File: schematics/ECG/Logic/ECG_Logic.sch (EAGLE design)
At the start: 72 parts, among them IC1 ADS1293, IC2 LIS3DH, IC3 MCP1703, IC4 CC2541, IC5 FSA4157, IC6 FSA4157, IC7 FSA4157, IC8 BALUN_2450BM_SERIES_SMD, X1 XTAL-2SMD, X2 XTAL_403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

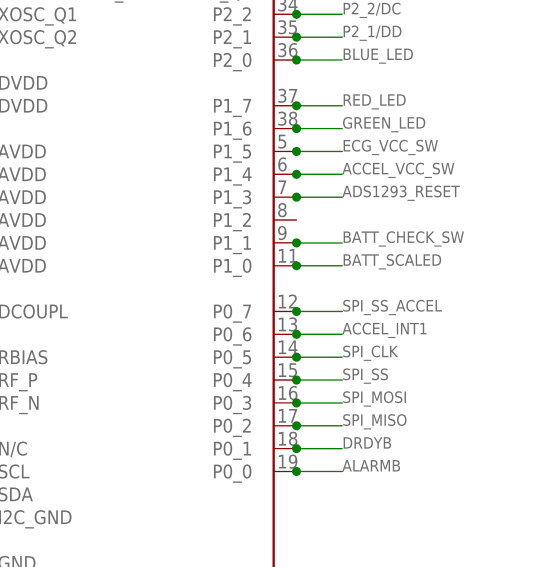
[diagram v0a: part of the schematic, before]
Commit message: moved batt scaled wire to ADC port 0 pin, updated routing. new gerbers generated for ordering v1.0 board
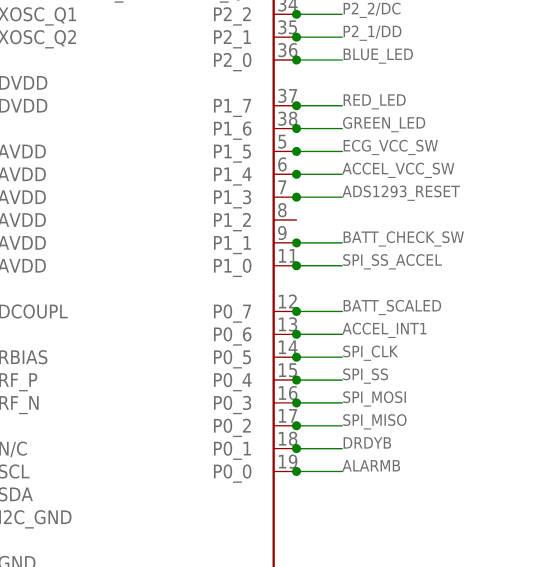
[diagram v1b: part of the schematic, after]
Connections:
- net BATT_SCALED: now also IC4.P0_7; no longer IC4.P1_0
- net SPI_SS_ACCEL: now also IC4.P1_0; no longer IC4.P0_7
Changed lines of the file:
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@@
 <grid distance="0.1" unitdist="inch" unit="inch" style="lines" multiple="1" display="no" altdistance="0.01" altunitdist="inch" altunit="inch"/>
 <layers>
-<layer number="1" name="Top" color="4" fill="1" visible="yes" active="no"/>
-<layer number="2" name="Route2" color="1" fill="3" visible="yes" active="no"/>
-<layer number="3" name="Route3" color="4" fill="3" visible="yes" active="no"/>
-<layer number="4" name="Route4" color="1" fill="4" visible="yes" active="no"/>
-<layer number="5" name="Route5" color="4" fill="4" visible="yes" active="no"/>
-<layer number="6" name="Route6" color="1" fill="8" visible="yes" active="no"/>
-<layer number="7" name="Route7" color="4" fill="8" visible="yes" active="no"/>
-<layer number="8" name="Route8" color="1" fill="2" visible="yes" active="no"/>
-<layer number="9" name="Route9" color="4" fill="2" visible="yes" active="no"/>
-<layer number="10" name="Route10" color="1" fill="7" visible="yes" active="no"/>
-<layer number="11" name="Route11" color="4" fill="7" visible="yes" active="no"/>
-<layer number="12" name="Route12" color="1" fill="5" visible="yes" active="no"/>
-<layer number="13" name="Route13" color="4" fill="5" visible="yes" active="no"/>
-<layer number="14" name="Route14" color="1" fill="6" visible="yes" active="no"/>
-<layer number="15" name="Route15" color="4" fill="6" visible="yes" active="no"/>
-<layer number="16" name="Bottom" color="1" fill="1" visible="yes" active="no"/>
-<layer number="17" name="Pads" color="2" fill="1" visible="yes" active="no"/>
-<layer number="18" name="Vias" color="2" fill="1" visible="yes" active="no"/>
-<layer number="19" name="Unrouted" color="6" fill="1" visible="yes" active="no"/>
-<layer number="20" name="Dimension" color="15" fill="1" visible="yes" active="no"/>
-<layer number="21" name="tPlace" color="7" fill="1" visible="yes" active="no"/>
-<layer number="22" name="bPlace" color="7" fill="1" visible="yes" active="no"/>
-<layer number="23" name="tOrigins" color="15" fill="1" visible="yes" active="no"/>
-<layer number="24" name="bOrigins" color="15" fill="1" visible="yes" active="no"/>
-<layer number="25" name="tNames" color="7" fill="1" visible="yes" active="no"/>
-<layer number="26" name="bNames" color="7" fill="1" visible="yes" active="no"/>
-<layer number="27" name="tValues" color="7" fill="1" visible="yes" active="no"/>
-<layer number="28" name="bValues" color="7" fill="1" visible="yes" active="no"/>
+<layer number="1" name="Top" color="4" fill="1" visible="no" active="no"/>
+<layer number="2" name="Route2" color="1" fill="3" visible="no" active="no"/>
+<layer number="3" name="Route3" color="4" fill="3" visible="no" active="no"/>
+<layer number="4" name="Route4" color="1" fill="4" visible="no" active="no"/>
+<layer number="5" name="Route5" color="4" fill="4" visible="no" active="no"/>
+<layer number="6" name="Route6" color="1" fill="8" visible="no" active="no"/>
+<layer number="7" name="Route7" color="4" fill="8" visible="no" active="no"/>
+<layer number="8" name="Route8" color="1" fill="2" visible="no" active="no"/>
+<layer number="9" name="Route9" color="4" fill="2" visible="no" active="no"/>
+<layer number="10" name="Route10" color="1" fill="7" visible="no" active="no"/>
+<layer number="11" name="Route11" color="4" fill="7" visible="no" active="no"/>
+<layer number="12" name="Route12" color="1" fill="5" visible="no" active="no"/>
+<layer number="13" name="Route13" color="4" fill="5" visible="no" active="no"/>
+<layer number="14" name="Route14" color="1" fill="6" visible="no" active="no"/>
+<layer number="15" name="Route15" color="4" fill="6" visible="no" active="no"/>
+<layer number="16" name="Bottom" color="1" fill="1" visible="no" active="no"/>
+<layer number="17" name="Pads" color="2" fill="1" visible="no" active="no"/>
+<layer number="18" name="Vias" color="2" fill="1" visible="no" active="no"/>
+<layer number="19" name="Unrouted" color="6" fill="1" visible="no" active="no"/>
+<layer number="20" name="Dimension" color="15" fill="1" visible="no" active="no"/>
+<layer number="21" name="tPlace" color="7" fill="1" visible="no" active="no"/>
+<layer number="22" name="bPlace" color="7" fill="1" visible="no" active="no"/>
+<layer number="23" name="tOrigins" color="15" fill="1" visible="no" active="no"/>
+<layer number="24" name="bOrigins" color="15" fill="1" visible="no" active="no"/>
+<layer number="25" name="tNames" color="7" fill="1" visible="no" active="no"/>
+<layer number="26" name="bNames" color="7" fill="1" visible="no" active="no"/>
+<layer number="27" name="tValues" color="7" fill="1" visible="no" active="no"/>
+<layer number="28" name="bValues" color="7" fill="1" visible="no" active="no"/>
 <layer number="29" name="tStop" color="7" fill="3" visible="no" active="no"/>
 <layer number="30" name="bStop" color="7" fill="6" visible="no" active="no"/>
@@
 <layer number="35" name="tGlue" color="7" fill="4" visible="no" active="no"/>
 <layer number="36" name="bGlue" color="7" fill="5" visible="no" active="no"/>
-<layer number="37" name="tTest" color="7" fill="1" visible="yes" active="no"/>
-<layer number="38" name="bTest" color="7" fill="1" visible="yes" active="no"/>
+<layer number="37" name="tTest" color="7" fill="1" visible="no" active="no"/>
+<layer number="38" name="bTest" color="7" fill="1" visible="no" active="no"/>
 <layer number="39" name="tKeepout" color="4" fill="11" visible="no" active="no"/>
 <layer number="40" name="bKeepout" color="1" fill="11" visible="no" active="no"/>
@@
 <layer number="44" name="Drills" color="7" fill="1" visible="no" active="no"/>
 <layer number="45" name="Holes" color="7" fill="1" visible="no" active="no"/>
-<layer number="46" name="Milling" color="3" fill="1" visible="yes" active="no"/>
-<layer number="47" name="Measures" color="7" fill="1" visible="yes" active="no"/>
-<layer number="48" name="Document" color="7" fill="1" visible="yes" active="no"/>
-<layer number="49" name="Reference" color="7" fill="1" visible="yes" active="no"/>
-<layer number="50" name="dxf" color="7" fill="1" visible="yes" active="no"/>
-<layer number="51" name="tDocu" color="7" fill="1" visible="yes" active="no"/>
-<layer number="52" name="bDocu" color="7" fill="1" visible="yes" active="no"/>
-<layer number="53" name="tGND_GNDA" color="7" fill="9" visible="yes" active="no"/>
-<layer number="54" name="bGND_GNDA" color="1" fill="9" visible="yes" active="no"/>
-<layer number="56" name="wert" color="7" fill="1" visible="yes" active="no"/>
+<layer number="46" name="Milling" color="3" fill="1" visible="no" active="no"/>
+<layer number="47" name="Measures" color="7" fill="1" visible="no" active="no"/>
+<layer number="48" name="Document" color="7" fill="1" visible="no" active="no"/>
+<layer number="49" name="Reference" color="7" fill="1" visible="no" active="no"/>
+<layer number="50" name="dxf" color="7" fill="1" visible="no" active="no"/>
+<layer number="51" name="tDocu" color="7" fill="1" visible="no" active="no"/>
+<layer number="52" name="bDocu" color="7" fill="1" visible="no" active="no"/>
+<layer number="53" name="tGND_GNDA" color="7" fill="9" visible="no" active="no"/>
+<layer number="54" name="bGND_GNDA" color="1" fill="9" visible="no" active="no"/>
+<layer number="56" name="wert" color="7" fill="1" visible="no" active="no"/>
 <layer number="91" name="Nets" color="2" fill="1" visible="yes" active="yes"/>
 <layer number="92" name="Busses" color="1" fill="1" visible="yes" active="yes"/>
@@
 </segment>
 <segment>
-<pinref part="IC4" gate="G$1" pin="P1_0"/>
-<wire x1="243.84" y1="101.6" x2="248.92" y2="101.6" width="0.1524" layer="91"/>
-<junction x="243.84" y="101.6"/>
-<label x="248.92" y="101.6" size="1.27" layer="95"/>
+<pinref part="IC4" gate="G$1" pin="P0_7"/>
+<wire x1="243.84" y1="96.52" x2="248.92" y2="96.52" width="0.1524" layer="91"/>
+<junction x="243.84" y="96.52"/>
+<label x="248.92" y="96.52" size="1.27" layer="95"/>
 </segment>
 </net>
@@
 </segment>
 <segment>
-<pinref part="IC4" gate="G$1" pin="P0_7"/>
-<wire x1="243.84" y1="96.52" x2="248.92" y2="96.52" width="0.1524" layer="91"/>
-<junction x="243.84" y="96.52"/>
-<label x="248.92" y="96.52" size="1.27" layer="95"/>
-</segment>
-</net>
+<pinref part="IC4" gate="G$1" pin="P1_0"/>
+<wire x1="243.84" y1="101.6" x2="248.92" y2="101.6" width="0.1524" layer="91"/>
+<junction x="243.84" y="101.6"/>
+<label x="248.92" y="101.6" size="1.27" layer="95"/>
+</segment>
+</net>

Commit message: added comments to board
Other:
- note added: "add 47uF cap to batt+"
- note added: "add batt/gnd pads"
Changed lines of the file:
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@@
 <text x="182.88" y="40.64" size="1.27" layer="95">32MHz</text>
 <text x="236.22" y="40.64" size="1.27" layer="95">32.768KHz</text>
+<text x="2.54" y="228.6" size="1.778" layer="91">add 47uF cap to batt+</text>
+<text x="2.54" y="226.06" size="1.778" layer="91">add batt/gnd pads</text>
 </plain>
 <instances>
